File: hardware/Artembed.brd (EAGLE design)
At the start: 94 x 36.5 mm, 75 parts, among them J2 CORTEX_JTAG_DEBUG_MINIMUM_PTH, J3 CORTEX_JTAG_DEBUG_PTH_NS, J5 1X04_SMD_STRAIGHT_COMBO, J6 QWIIC_RIGHT_ANGLE, J7 CAMERA-HIMAX, J9 1X04_SMD_STRAIGHT_COMBO, U1 DAPLINK_KL26Z, U2 ARTEMIS_MODULESMD, U3 LIS2DH12, U4 AP2127K-1.8V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

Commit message: checkpoint
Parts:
- moved C18 10.2 mm to (47.0, 7.62)
- moved C19 10.2 mm to (47.0, 12.7)
- moved U4 10.2 mm to (47.0, 10.2)
- moved C15 9.94 mm to (11.3, 28.8), turned to 90 degrees
- moved J2 7.10 mm to (21.6, 30.5), turned to 270 degrees
- moved U3 6.51 mm to (15.4, 33.7), turned to 90 degrees
- moved R15 5.00 mm to (9.91, 33.7), turned to 90 degrees
- moved E1 4.66 mm to (14.5, 28.8), turned to 90 degrees
- moved C1 2.54 mm to (34.9, 18.4)
- moved C10 2.54 mm to (41.9, 18.4)
- moved C11 2.54 mm to (36.8, 18.4)
- moved C2 2.54 mm to (33.5, 18.4)
- moved C3 2.54 mm to (32.1, 18.4)
- moved U2 2.54 mm to (36.8, 27.9)
- moved Y1 2.54 mm to (39.4, 18.4)
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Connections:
- removed net VDD: R14.2, R15.2
- net 3.3V: now also R14.2, R15.2
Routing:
- net SDA: track 0.00 -> 63.9 mm, vias 0 -> 3
- net SCL: track 0.00 -> 62.2 mm, vias 0 -> 4
- net CAMERA_D0: track 2.98 -> 47.7 mm, vias 1 -> 2
- net CAMERA_PCLK: track 2.87 -> 45.4 mm, vias 1 -> 3
- net CAMERA_D4: track 3.61 -> 44.8 mm, vias 1 -> 2
- net CAMERA_D2: track 3.06 -> 43.5 mm, vias 1 -> 2
- net CAMERA_HSYNC: track 2.26 -> 41.3 mm, vias 1 -> 2
- net TGT_SWO: track 0.64 -> 39.7 mm, vias 0 -> 3
- net !TGT_RST: track 33.2 -> 69.2 mm, vias 0 -> 3
- net CAMERA_D5: track 1.97 -> 35.3 mm, vias 1 -> 2
- net CAMERA_D3: track 3.22 -> 36.4 mm, vias 1 -> 2
- net CAMERA_TRIG: track 2.59 -> 34.3 mm, vias 1 -> 2
- net CAMERA_D1: track 3.00 -> 33.9 mm, vias 1 -> 2
- net CAMERA_D7: track 4.05 -> 33.0 mm, vias 1 -> 2
- net CAMERA_MCLK: track 1.80 -> 30.0 mm, vias 1 -> 2
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
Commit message: finished routing camera
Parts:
- moved R12 3.98 mm to (83.7, 10.2), turned to 225 degrees
- moved C4 2.84 mm to (85.1, 8.89), turned to 225 degrees
- moved C1 2.84 mm to (36.2, 15.9)
- moved C10 2.84 mm to (43.2, 15.9)
- moved C11 2.84 mm to (38.1, 15.9)
- moved C2 2.84 mm to (34.8, 15.9)
- moved C3 2.84 mm to (33.4, 15.9)
- moved Y1 2.84 mm to (40.6, 15.9)
- moved U2 1.27 mm to (38.1, 27.9)
- turned S2 to 315 degrees
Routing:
- net CAMERA_INT: track 1.67 -> 38.4 mm, vias 1 -> 2
- net CAMERA_D1: track 33.9 -> 50.7 mm
- net 3.3V: track 82.6 -> 98.1 mm, vias 4 -> 6
- net PDM_DATA: track 19.3 -> 34.2 mm
- net D25: track 4.70 -> 19.1 mm, vias 0 -> 1
- net D24: track 4.70 -> 18.6 mm, vias 0 -> 1
- net 1.8V: track 5.84 -> 18.9 mm, vias 0 -> 2
- net D27: track 4.70 -> 17.3 mm, vias 0 -> 1
- net D35: track 4.70 -> 17.3 mm, vias 0 -> 1
- net D39: track 6.39 -> 18.5 mm, vias 0 -> 1
- net D28: track 4.70 -> 16.5 mm, vias 0 -> 1
- net D26: track 4.70 -> 16.5 mm, vias 0 -> 1
- net D23_LED: track 4.70 -> 16.2 mm, vias 0 -> 1
- net CAMERA_MCLK: track 30.0 -> 40.9 mm
- net PDM_CLK: track 19.9 -> 30.7 mm
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
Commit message: routed gpio
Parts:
- moved J10 2.54 mm to (50.8, 27.9)
- moved J5 2.54 mm to (71.1, 27.9)
- moved C18 2.54 mm to (44.5, 7.62)
- moved C19 2.54 mm to (44.5, 12.7)
- moved J22 2.54 mm to (50.8, 34.3)
- moved J24 2.54 mm to (50.8, 36.8)
- moved J26 2.54 mm to (50.8, 32.4)
- moved U4 2.54 mm to (44.5, 10.2)
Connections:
- net D13: now also J11.1, J11.1@2, J14.5, J25.5; no longer J22.12, J26.12, J5.4, J5.4-2
- net D16: now also J22.12, J26.12, J5.4, J5.4-2; no longer J22.11, J26.11, J5.3, J5.3-2
- net D23_LED: now also J14.3, J25.3, J9.3, J9.3-2; no longer J10.4, J10.4@2, J22.4, J26.4
- net D24: now also J14.1, J25.1, J9.1, J9.1-2; no longer J10.3, J10.3@2, J22.3, J26.3
- net D25: now also J11.7, J11.7@2, J14.11, J25.11; no longer J10.2, J10.2@2, J22.2, J26.2
- net D26: now also J11.6, J11.6@2, J14.10, J25.10; no longer J10.1, J10.1@2, J22.1, J26.1
- net D27: now also J14.4, J25.4, J9.4, J9.4-2; no longer J11.8, J11.8@2, J14.12, J25.12
- net D28: now also J11.8, J11.8@2, J14.12, J25.12; no longer J11.7, J11.7@2, J14.11, J25.11
- net D29: now also J11.4, J11.4@2, J14.8, J25.8; no longer J22.10, J26.10, J5.2, J5.2-2
- net D31: now also J22.11, J26.11, J5.3, J5.3-2; no longer J22.9, J26.9, J5.1, J5.1-2
- net D32: now also J11.3, J11.3@2, J14.7, J25.7; no longer J10.8, J10.8@2, J22.8, J26.8
- net D33: now also J11.2, J11.2@2, J14.6, J25.6; no longer J10.7, J10.7@2, J22.7, J26.7
- net D34: now also J11.5, J11.5@2, J14.9, J25.9; no longer J10.6, J10.6@2, J22.6, J26.6
- net D35: now also J14.2, J25.2, J9.2, J9.2-2; no longer J10.5, J10.5@2, J22.5, J26.5
- net D36: now also J10.6, J10.6@2, J22.6, J26.6; no longer J11.6, J11.6@2, J14.10, J25.10
- net D37: now also J10.4, J10.4@2, J22.4, J26.4; no longer J11.5, J11.5@2, J14.9, J25.9
- net D38: now also J10.5, J10.5@2, J22.5, J26.5; no longer J11.4, J11.4@2, J14.8, J25.8
- net D39: now also J10.1, J10.1@2, J22.1, J26.1; no longer J11.3, J11.3@2, J14.7, J25.7
- net D40: now also J10.2, J10.2@2, J22.2, J26.2; no longer J11.2, J11.2@2, J14.6, J25.6
- net D41: now also J22.10, J26.10, J5.2, J5.2-2; no longer J11.1, J11.1@2, J14.5, J25.5
- net D42: now also J10.7, J10.7@2, J22.7, J26.7; no longer J14.4, J25.4, J9.4, J9.4-2
- net D43: now also J10.8, J10.8@2, J22.8, J26.8; no longer J14.3, J25.3, J9.3, J9.3-2
- net D44: now also J10.3, J10.3@2, J22.3, J26.3; no longer J14.2, J25.2, J9.2, J9.2-2
- net D45: now also J22.9, J26.9, J5.1, J5.1-2; no longer J14.1, J25.1, J9.1, J9.1-2
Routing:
- net !TGT_RST: track 62.1 -> 131.3 mm
- net D24: track 18.6 -> 59.3 mm, vias 1 -> 2
- net D35: track 17.3 -> 56.4 mm, vias 1 -> 2
- net D16: track 8.52 -> 45.5 mm
- net D31: track 7.62 -> 42.8 mm
- net D23_LED: track 16.2 -> 49.3 mm, vias 1 -> 2
- net D41: track 6.57 -> 39.1 mm
- net D45: track 7.39 -> 37.1 mm
- net D27: track 17.3 -> 47.0 mm, vias 1 -> 2
- net D32: track 7.96 -> 37.4 mm, vias 1 -> 2
- net D43: track 7.48 -> 36.7 mm
- net D13: track 14.1 -> 40.7 mm, vias 1 -> 2
- net D42: track 6.56 -> 33.1 mm
- net D36: track 6.63 -> 30.6 mm
- net D33: track 12.9 -> 36.5 mm, vias 1 -> 2
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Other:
- board size 94 x 36.5 mm -> 94 x 38.1 mm

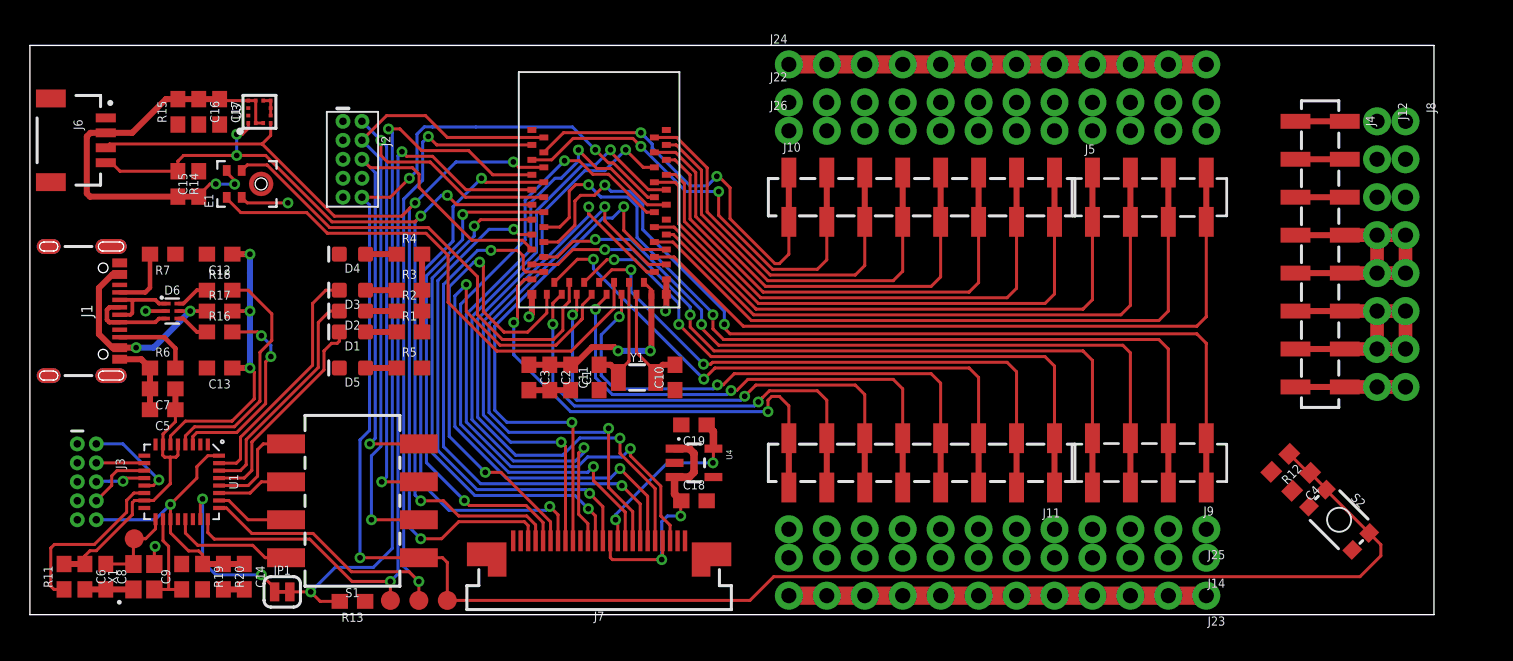
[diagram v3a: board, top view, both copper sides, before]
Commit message: ground purs and all airwires gone
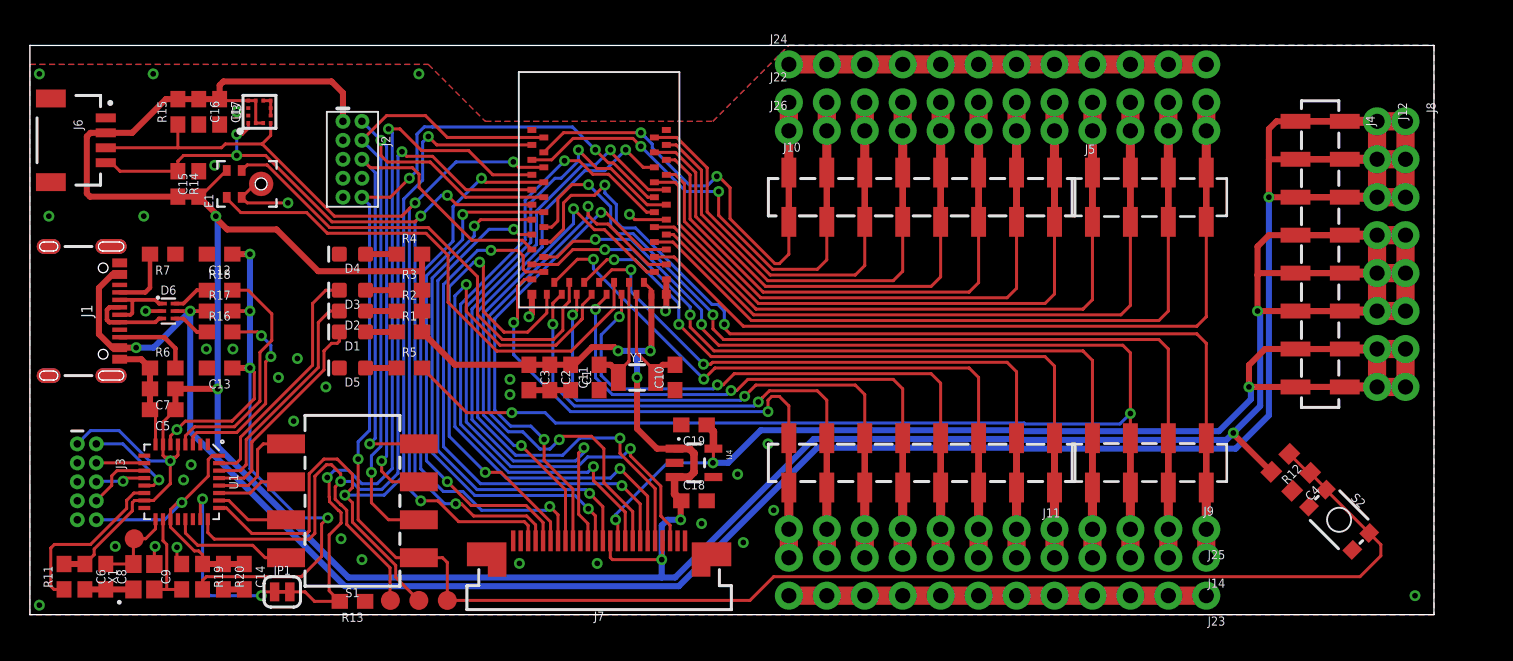
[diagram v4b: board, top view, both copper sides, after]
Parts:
- moved D6 0.25 mm to (9.27, 20.3)
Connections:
- net 1.8V: now also J12.7, J4.7, J4.7@2, J8.7
- net 3.3V: now also J12.4, J12.5, J4.4, J4.4@2, J4.5, J4.5@2, J8.4, J8.5; no longer J12.7, J4.7, J4.7@2, J8.7
- net VBUS_IF: now also J12.1, J12.2, J12.3, J4.1, J4.1@2, J4.2, J4.2@2, J4.3, J4.3@2, J8.1, J8.2, J8.3
- net VBUS_IF2: no longer J12.4, J12.5, J4.4, J4.4@2, J4.5, J4.5@2, J8.4, J8.5
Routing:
- net 3.3V: track 97.1 -> 286.9 mm, vias 6 -> 10
- net VBUS_IF: track 14.3 -> 160.8 mm, vias 2 -> 3
- net 1.8V: track 16.6 -> 79.1 mm, vias 2 -> 3
- net D23_LED: track 49.3 -> 106.6 mm, vias 2 -> 4
- net VBUS_IF2: track 33.8 -> 45.9 mm, vias 3 -> 5
- net GND: track 79.4 -> 90.4 mm, vias 5 -> 36
- net D24: track 59.3 -> 67.3 mm
- net D34: track 30.9 -> 38.9 mm
- net D28: track 29.1 -> 37.1 mm
- net D27: track 47.0 -> 55.0 mm
- net D26: track 30.2 -> 38.2 mm
- net D13: track 40.7 -> 48.7 mm
- net D40: track 27.7 -> 35.7 mm
- net D25: track 28.4 -> 36.4 mm
- net D45: track 37.1 -> 45.1 mm
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- added copper zone on layer 1, net GND
- added copper zone on layer 16, net GND

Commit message: added top silkscreen
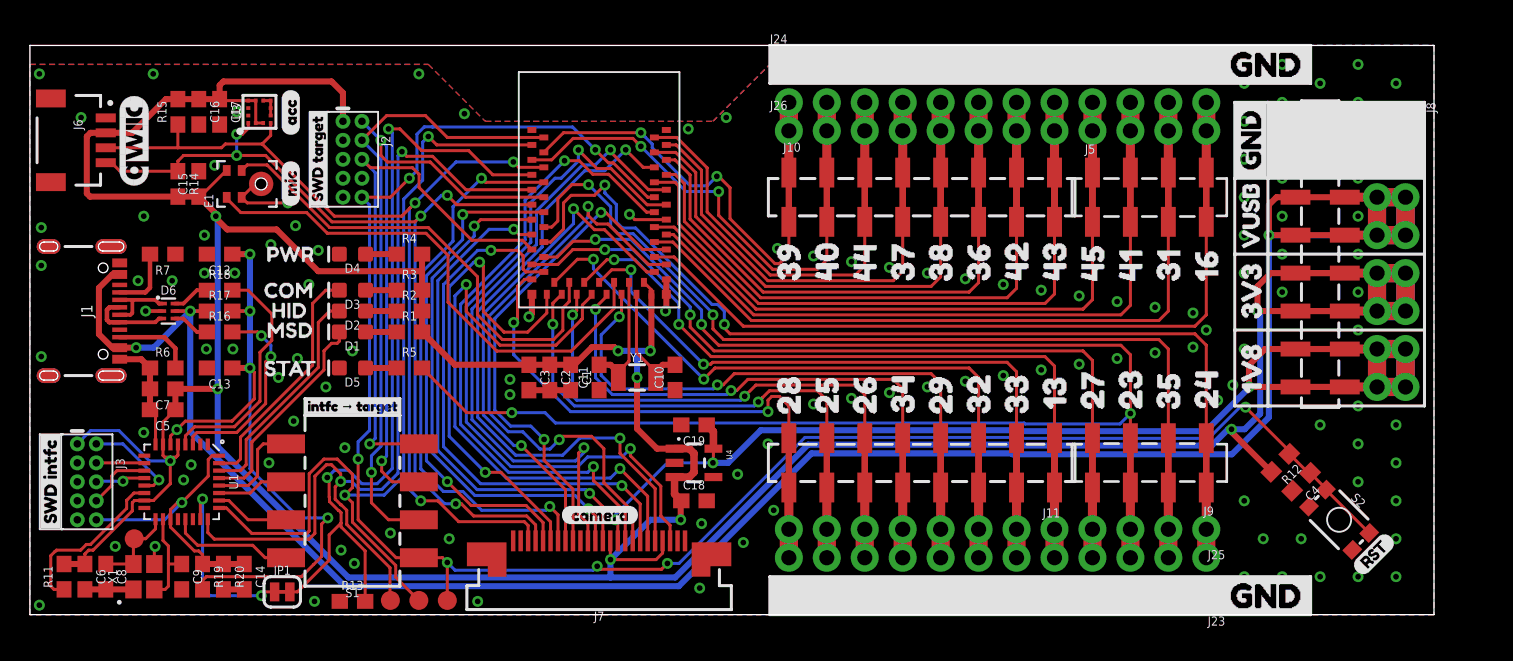
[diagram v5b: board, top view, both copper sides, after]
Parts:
- added U$1: (no value), 4mar2020_1:RST6
- added U$10: (no value), pin_labels:442
- added U$11: (no value), pin_labels:373
- added U$12: (no value), pin_labels:384
- added U$13: (no value), pin_labels:365
- added U$14: (no value), pin_labels:426
- added U$15: (no value), pin_labels:437
- added U$16: (no value), pin_labels:458
- added U$17: (no value), pin_labels:419
- added U$18: (no value), pin_labels:3110
- added U$19: (no value), pin_labels:1611
- added U$2, U$3: (no value), 4mar2020_1:GND0
- added U$20: (no value), pin_labels:2812
- added U$21: (no value), pin_labels:2513
- added U$22: (no value), pin_labels:2614
- added U$23: (no value), pin_labels:3415
- added U$24: (no value), pin_labels:2916
- added U$25: (no value), pin_labels:3217
- added U$26: (no value), pin_labels:3318
- added U$27: (no value), pin_labels:1319
- added U$28: (no value), pin_labels:2720
- added U$29: (no value), pin_labels:2321
- added U$30: (no value), pin_labels:3522
- added U$31: (no value), pin_labels:2423
- added U$32: (no value), SparkFun-Aesthetics:QWIIC_6MM
- added U$33: (no value), 4mar2020_1:SWD_TARGET7
- added U$34: (no value), 4mar2020_1:SWD_INTFC8
- added U$35: (no value), 4mar2020_1:CAMERA11
- added U$36: (no value), 4mar2020_1:MIC9
- added U$37: (no value), 4mar2020_1:ACC10
- added U$38: (no value), 4mar2020_1:INTFC##TARGET12
- added U$39: (no value), 4mar2020_1:PWR13
- added U$4: (no value), 4mar2020_1:GND2
- added U$40: (no value), 4mar2020_1:MSD16
- added U$41: (no value), 4mar2020_1:HID15
- added U$42: (no value), 4mar2020_1:COM14
- added U$43: (no value), 4mar2020_1:STAT17
- added U$5: (no value), 4mar2020_1:3V34
- added U$6: (no value), 4mar2020_1:1V85
- added U$7: (no value), 4mar2020_1:VUSB5
- added U$8: (no value), pin_labels:390
- added U$9: (no value), pin_labels:401
- J3: value CORTEX_JTAG_DEBUG_PTH_NS -> CORTEX_JTAG_DEBUG_PTH; device SparkFun-Connectors:2X5-PTH-1.27MM-NO_SILK -> SparkFun-Connectors:2X5-PTH-1.27MM
- turned C9 to 270 degrees
- turned R13 to 0 degrees
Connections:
- net 3.3V: no longer J12.4, J4.4, J4.4@2, J8.4
- net GND: now also J12.1, J12.2, J4.1, J4.1@2, J4.2, J4.2@2, J8.1, J8.2
- net VBUS_IF: now also J12.4, J4.4, J4.4@2, J8.4; no longer J12.1, J12.2, J4.1, J4.1@2, J4.2, J4.2@2, J8.1, J8.2
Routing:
- net GND: track 90.4 -> 106.9 mm, vias 36 -> 122
- net VBUS_IF: track 160.8 -> 151.1 mm
- net 1.8V: track 79.1 -> 87.4 mm
- net 3.3V: track 286.9 -> 281.0 mm
- net TGT_BOOT: track 52.0 -> 54.7 mm
- net !TGT_RST: track 129.9 -> 127.1 mm, vias 3 -> 7

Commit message: add info silk, ran checklist
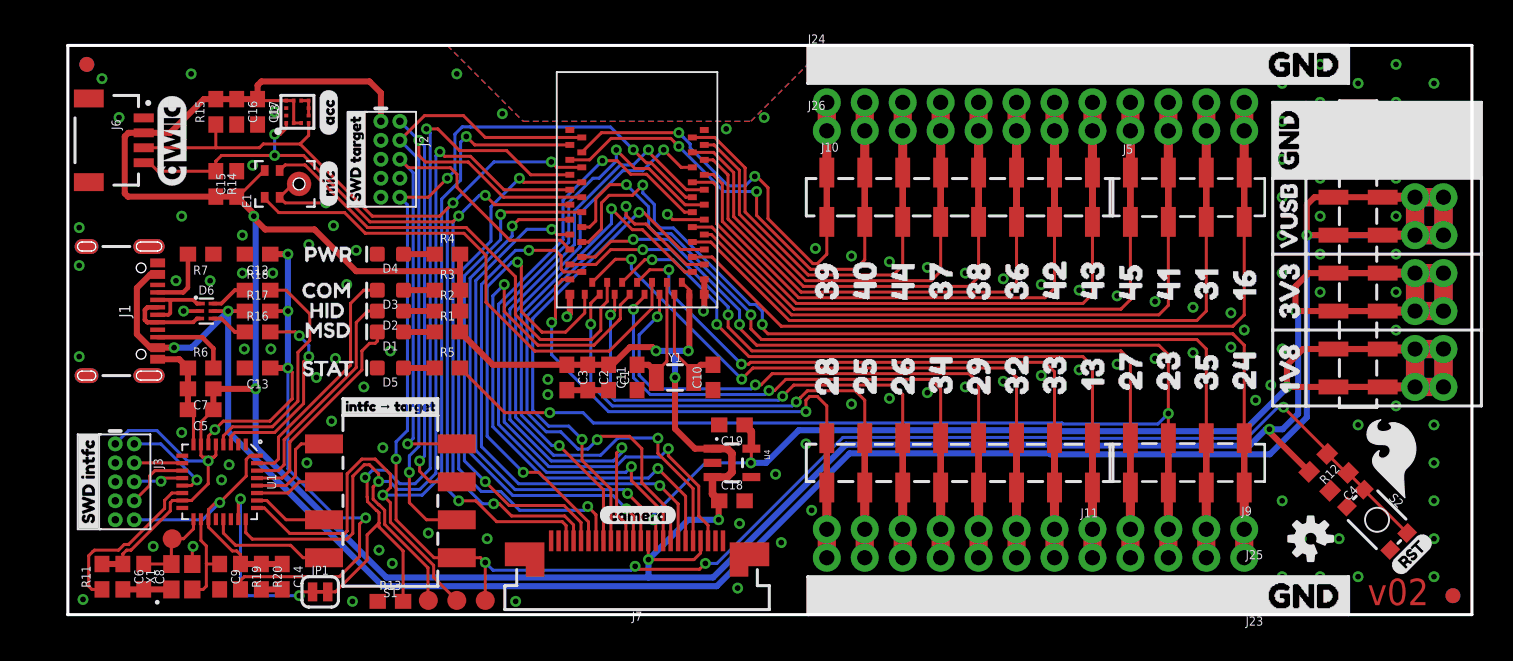
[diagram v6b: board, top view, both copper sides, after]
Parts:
- added FD1, FD2, FD3, FD4: FIDUCIAL1X2, SparkFun-Aesthetics:FIDUCIAL-1X2
- added LOGO1: OSHW-LOGOS, SparkFun-Aesthetics:OSHW-LOGO-S
- added LOGO2: SFE_LOGO_NAME_FLAME.2_INCH, SparkFun-Aesthetics:SFE_LOGO_NAME_FLAME_.2
- added U$100: (no value), info:PWM7
- added U$101, U$137, U$69: (no value), pin_labels:2321
- added U$102, U$140: (no value), info:TX9
- added U$103, U$132: (no value), info:RX10
- added U$104: (no value), info:UART18
- added U$105, U$71: (no value), pin_labels:2423
- added U$106, U$122, U$61, U$98: (no value), pin_labels:2513
- added U$107, U$138, U$62: (no value), pin_labels:2614
- added U$108, U$141, U$68, U$97: (no value), pin_labels:2720
- added U$109, U$142, U$60, U$99: (no value), pin_labels:2812
- added U$110, U$124, U$51: (no value), pin_labels:373
- added U$111, U$126, U$143, U$48, U$96: (no value), pin_labels:390
- added U$112, U$128, U$54, U$93: (no value), pin_labels:426
- added U$113, U$129, U$55, U$92: (no value), pin_labels:437
- added U$114, U$145, U$50, U$94: (no value), pin_labels:442
- added U$115, U$147, U$56: (no value), pin_labels:458
- added U$116, U$130, U$67, U$77: (no value), pin_labels:1319
- added U$117, U$134, U$64, U$79: (no value), pin_labels:2916
- added U$118, U$135, U$58, U$80: (no value), pin_labels:3110
- added U$119, U$65, U$81: (no value), pin_labels:3217
- added U$120, U$66, U$82: (no value), pin_labels:3318
- added U$121, U$131, U$70, U$84: (no value), pin_labels:3522
- added U$123, U$53: (no value), pin_labels:365
- added U$125, U$52, U$91: (no value), pin_labels:384
- added U$127, U$144, U$49, U$95: (no value), pin_labels:401
- added U$133, U$59, U$78: (no value), pin_labels:1611
- added U$136, U$63, U$83: (no value), pin_labels:3415
- added U$139: (no value), info:UART011
- added U$146, U$57: (no value), pin_labels:419
- added U$148, U$149: (no value), 4mar2020_1:GND0
- added U$45: (no value), SparkFun-Aesthetics:SFE_LOGO_FLAME_.2
- added U$47: (no value), 4mar2020_1:ARTMBED17
- added U$72: (no value), 4mar2020_1:GND1
- added U$73: (no value), 4mar2020_1:1V83
- added U$74: (no value), 4mar2020_1:3V32
- added U$75: (no value), 4mar2020_1:VUSB4
- added U$76: (no value), info:ADC0
- added U$85: (no value), info:IOM21
- added U$86: (no value), info:IOM32
- added U$87: (no value), info:IOM43
- added U$88: (no value), info:SCL#SCLK4
- added U$89: (no value), info:SDA#MISO5
- added U$90: (no value), info:MOSI6
- moved FRAME1 108.7 mm to (25.4, -12.7)
- moved U$20 2.84 mm to (53.3, 13.3)
- moved U$25 2.84 mm to (66.0, 13.3)
- moved U$13 2.84 mm to (66.0, 19.7)
- moved U$15 2.84 mm to (71.1, 19.7)
- moved U$17 2.84 mm to (76.2, 19.7)
- moved U$19 2.84 mm to (81.3, 19.7)
- moved U$27 2.84 mm to (71.1, 13.7)
- moved U$29 2.84 mm to (76.2, 13.7)
- moved U$31 2.84 mm to (81.3, 13.7)
- moved U$8 2.84 mm to (53.3, 19.7)
- moved U$21 2.84 mm to (55.9, 13.3)
- moved U$22 2.84 mm to (58.4, 13.3)
- moved U$23 2.84 mm to (61.0, 13.3)
- moved U$24 2.84 mm to (63.5, 13.3)
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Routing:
- net GND: vias 122 -> 121
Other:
- board text added: "Owen Lyke, Kyle Wenner"
- board text added: "v02"
